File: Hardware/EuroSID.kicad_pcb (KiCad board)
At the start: 2 copper layers, 213.3 x 106.6 mm, 204 parts, among them J1 GATE_2, J10 IN_2, J11 IN_3, J12 PWM_CV, J13 Conn_01x04_Female, J14 Eurorack Connector, J15 Conn_01x06_Male, J16 Conn_ARM_JTAG_SWD_10, J2 GATE_3, J3 GATE_1, J4 OUT2_CON, J5 EXT_CON, J6 CUTOFF_CV, J7 SHAPE_CV, J8 OUT1_CON, J9 IN_1, Q1 MMBT3904, Q2 MMBT3904, Q3 MMBT3904, SW1 Frequency Adjust, SW10 FILTER_SW, SW11 FILTEREXT_SW, SW2 MOD_SW, SW3 FILTER1_SW, SW4 VOICE_SW, SW5 FILTER2_SW, SW6 PROG, SW7 RST, SW8 MODE_SW, SW9 FILTER3_SW, U1 TLC5947DAP, U10 LM1117-5.0, U11 L7809, U12 STM32F030R8Tx, U13 LM1117-3.3, U2 MCP6002-xSN, U3 MCP6004, U4 OPA1678, U5 MCP6002-xSN, U6 74HC595, U7 74HC595, U8 SID, U9 LM1117-3.3, X1 ECS-8FMX-010-TR

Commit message: Updated schematic
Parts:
- removed D28: LM4040DBZ-10, Package_TO_SOT_SMD:SOT-23
- added C69: 4.7 uF, Capacitor_Tantalum_SMD:CP_EIA-3216-18_Kemet-A, F.Cu at (107.4, 110.5)
- added D19: LP, LED_THT:LED_D3.0mm, F.Cu at (219.7, 49.5)
- added J17: Conn_ARM_JTAG_SWD_10, Connector_PinHeader_2.54mm:PinHeader_2x05_P2.54mm_Vertical, F.Cu at (59.7, 41.9)
- added R52: 120k, Resistor_SMD:R_0603_1608Metric, F.Cu at (135.9, 134.6)
- added R53: 1k, Resistor_SMD:R_0603_1608Metric, F.Cu at (110.4, 110.5)
- added R54: 1k, Resistor_SMD:R_0603_1608Metric, F.Cu at (107.4, 112.0)
- added R55: 1k, Resistor_SMD:R_0603_1608Metric, F.Cu at (110.4, 112.0)
- added SW12: FILTEREXT_SW, Button_Switch_THT:SW_PUSH_6mm_H9.5mm, F.Cu at (167.6, 86.4)
- C13, C22: value 18 pF -> 100 nF
- C14: value 100 nF -> 18 pF
- C23, C24: value 3.3 nF -> 100 nF
- C25, C26: value 2.2 nF -> 100 nF
- C27: value 2.2 nF -> 18 pF
- C29, C30: value 1 uF -> 3.3 nF; footprint Capacitor_Tantalum_SMD:CP_EIA-2012-12_Kemet-R -> Capacitor_SMD:C_0603_1608Metric
- C31: value 100 nF -> 2.2 nF
- C32: value 2200 uF -> 2.2 nF; footprint Capacitor_SMD:CP_Elec_10x10 -> Capacitor_SMD:C_0603_1608Metric
- C33: value 22 uF -> 2.2 nF; footprint Capacitor_SMD:CP_Elec_4x5.3 -> Capacitor_SMD:C_0603_1608Metric
- C34: value 22 uF -> 3.3 nF; footprint Capacitor_SMD:CP_Elec_4x5.3 -> Capacitor_SMD:C_0603_1608Metric
- C35, C36: value 22 uF -> 1 uF; footprint Capacitor_SMD:CP_Elec_4x5.3 -> Capacitor_Tantalum_SMD:CP_EIA-2012-12_Kemet-R
- C37, C47: value 22 uF -> 100 nF; footprint Capacitor_SMD:CP_Elec_4x5.3 -> Capacitor_SMD:C_0603_1608Metric
- C38: value 22 uF -> 2200 uF; footprint Capacitor_SMD:CP_Elec_4x5.3 -> Capacitor_SMD:CP_Elec_10x10
- C39, C40, C41, C44, C51: value 100 nF -> 22 uF; footprint Capacitor_SMD:C_0603_1608Metric -> Capacitor_SMD:CP_Elec_4x5.3
- C45: value 0.1 uF -> 22 uF; footprint Capacitor_SMD:C_0603_1608Metric -> Capacitor_SMD:CP_Elec_4x5.3
- C5: value 100 nF -> 0.1 uF
- C52: value 4.7 uF -> 22 uF; footprint Capacitor_Tantalum_SMD:CP_EIA-3216-18_Kemet-A -> Capacitor_SMD:CP_Elec_4x5.3
- C54: value 10 nF -> 100 nF
- C57, C65: value 100 nF -> 4.7 uF; footprint Capacitor_SMD:C_0603_1608Metric -> Capacitor_Tantalum_SMD:CP_EIA-3216-18_Kemet-A
- C58: value 1 uF -> 100 nF; footprint Capacitor_Tantalum_SMD:CP_EIA-2012-12_Kemet-R -> Capacitor_SMD:C_0603_1608Metric
- C59: value 10 uF -> 10 nF; footprint Capacitor_SMD:CP_Elec_4x5.7 -> Capacitor_SMD:C_0603_1608Metric
- C60: value 4.7 uF -> 100 nF; footprint Capacitor_Tantalum_SMD:CP_EIA-3216-18_Kemet-A -> Capacitor_SMD:C_0603_1608Metric
- C63: value 100 nF -> 1 uF; footprint Capacitor_SMD:C_0603_1608Metric -> Capacitor_Tantalum_SMD:CP_EIA-2012-12_Kemet-R
- C64: value 4.7 uF -> 10 uF; footprint Capacitor_Tantalum_SMD:CP_EIA-3216-18_Kemet-A -> Capacitor_SMD:CP_Elec_4x5.7
- D10: value BP -> TRIANGLE
- D11: value TRIANGLE -> DECAY
- D12: value DECAY -> VOICE3
- D13: value VOICE3 -> SID2
- D14: value SID2 -> FILTEREXT
- D15: value FILTEREXT -> MOD
- D16: value MOD -> SAW
- D17: value SAW -> SUSTAIN
- D18: value SUSTAIN -> FILTER1
- D2: value MODE_RG -> FILTER2; footprint LED_THT:LED_D3.0mm-3 -> LED_THT:LED_D3.0mm
- D20: value FILTER1 -> SYNC
- D21: value LP -> SYNC
- D22: value SYNC -> RELEASE
- D23: value SYNC -> MODE_RG; footprint LED_THT:LED_D3.0mm -> LED_THT:LED_D3.0mm-3
- D24: value RELEASE -> BZT52-C5V1J; footprint LED_THT:LED_D3.0mm -> Diode_SMD:D_SOD-123
- D25: value BZT52-C5V1J -> 1N5819HW-7-F
- D27: value 1N5819HW-7-F -> LM4040DBZ-10; footprint Diode_SMD:D_SOD-123 -> Package_TO_SOT_SMD:SOT-23
- D3: value FILTER2 -> HP
- D4: value HP -> SQUARE
- D5: value SQUARE -> ATTACK
- D6: value ATTACK -> VOICE2
- D7: value VOICE2 -> SID1
- D8: value SID1 -> FILTER3
- D9: value FILTER3 -> BP
- J13: value Conn_01x04_Female -> EXT_CON; footprint Connector_PinHeader_2.54mm:PinHeader_1x04_P2.54mm_Vertical -> Connector_Audio:Jack_3.5mm_QingPu_WQP-PJ398SM_Vertical_CircularHoles
- J14: value Eurorack Connector -> Conn_01x04_Female; footprint Connector_PinHeader_2.54mm:PinHeader_2x08_P2.54mm_Vertical -> Connector_PinHeader_2.54mm:PinHeader_1x04_P2.54mm_Vertical
- J15: value Conn_01x06_Male -> Eurorack Connector; footprint Connector_PinHeader_2.54mm:PinHeader_1x06_P2.54mm_Vertical -> Connector_PinHeader_2.54mm:PinHeader_2x08_P2.54mm_Vertical
- J16: value Conn_ARM_JTAG_SWD_10 -> Conn_01x06_Male; footprint Connector_PinHeader_2.54mm:PinHeader_2x05_P2.54mm_Vertical -> Connector_PinHeader_2.54mm:PinHeader_1x06_P2.54mm_Vertical
- J5: value EXT_CON -> CUTOFF_CV
- J6: value CUTOFF_CV -> SHAPE_CV
- J7: value SHAPE_CV -> SET_CV
- R25: value 30k -> 10k
- R26: value 1k -> 30k
- R27: value 50k -> 1k
- R35, R48: value 120k -> 100k
- R36, R51: value 1k -> 120k
- R37: value 180k -> 120k
- R38: value 100k -> 120k
- R39: value 180k -> 1k
- R40: value 100k -> 50k
- R43: value 120k -> 180k
- R45: value 47k -> 180k
- R46: value 47k -> 100k
- R49, R50: value 1k -> 47k
- RV6: value DECAY -> SUSTAIN
- RV7: value SUSTAIN -> DECAY
- SW10: value FILTER_SW -> SET_SW
- SW11: value FILTEREXT_SW -> FILTER_SW
- SW4: value VOICE_SW -> PROG; footprint Button_Switch_THT:SW_PUSH_6mm_H9.5mm -> Button_Switch_SMD:SW_SPST_EVPBF
- SW5: value FILTER2_SW -> VOICE_SW
- SW6: value PROG -> FILTER2_SW; footprint Button_Switch_SMD:SW_SPST_EVPBF -> Button_Switch_THT:SW_PUSH_6mm_H9.5mm
- U10: value LM1117-5.0 -> LM1117-3.3
- U11: value L7809 -> LM1117-5.0; footprint Package_TO_SOT_SMD:TO-252-3_TabPin2 -> Package_TO_SOT_SMD:SOT-223-3_TabPin2
- U12: value STM32F030R8Tx -> L7809; footprint Package_QFP:LQFP-64_10x10mm_P0.5mm -> Package_TO_SOT_SMD:TO-252-3_TabPin2
- U13: value LM1117-3.3 -> STM32F030R8Tx; footprint Package_TO_SOT_SMD:SOT-223-3_TabPin2 -> Package_QFP:LQFP-64_10x10mm_P0.5mm
- U2, U5: value MCP6002-xSN -> OPA1678
- U4: value OPA1678 -> MCP6004; footprint Package_SO:SOIC-8_3.9x4.9mm_P1.27mm -> Package_SO:TSSOP-14_4.4x5mm_P0.65mm
- moved SW6 188.5 mm to (48.3, 87.6)
- moved R12 165.4 mm to (72.6, 64.1)
- moved R15 165.4 mm to (72.6, 62.6)
- moved R19 165.4 mm to (54.5, 62.6)
- moved R2 165.4 mm to (54.5, 64.1)
- moved R22 165.4 mm to (63.6, 62.6)
- moved R6 165.4 mm to (63.6, 64.1)
- moved R1 165.4 mm to (60.6, 62.6)
- moved R11 165.4 mm to (75.6, 62.6)
- moved R14 165.4 mm to (69.6, 64.1)
- moved R16 165.4 mm to (69.6, 62.6)
- moved R17 165.4 mm to (66.6, 64.1)
- moved R20 165.4 mm to (66.6, 62.6)
- moved R23 165.4 mm to (60.6, 64.1)
- moved R3 165.4 mm to (57.5, 62.6)
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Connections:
- C10 pad 1: CUTOFF -> +3.3VA
- C11 pad 1: +3.3VA -> GND
- C12 pad 1: GND -> +3.3VA
- C13 pad 1: Net-(C13-Pad1) -> GND
- C13 pad 2: Net-(C13-Pad2) -> GND
- C14 pad 1: ATTACK -> Net-(C14-Pad1)
- C14 pad 2: GND -> Net-(C14-Pad2)
- C15 pad 1: DECAY -> ATTACK
- C17 pad 1: +12V -> DECAY
- C18 pad 1: GND -> +3.3VA
- C18 pad 2: -12V -> GND
- C19 pad 1: RELEASE -> GND
- C20 pad 1: +12V -> RELEASE
- C21 pad 1: GND -> +3.3VA
- C21 pad 2: -12V -> GND
- C22 pad 1: Net-(C22-Pad1) -> GND
- C22 pad 2: Net-(C22-Pad2) -> GND
- C23 pad 1: SHAPE_CV -> +12V
- C23 pad 2: Net-(C23-Pad2) -> GND
- C24 pad 1: CUTOFF_CV -> GND
- C24 pad 2: Net-(C24-Pad2) -> -12V
- C25 pad 1: IN1_CV -> +12V
- C25 pad 2: Net-(C25-Pad2) -> GND
- C26 pad 1: IN2_CV -> GND
- C26 pad 2: Net-(C26-Pad2) -> -12V
- C27 pad 1: IN3_CV -> Net-(C27-Pad1)
- C28 pad 1: PWM_CV -> SHAPE_CV
- C29 pad 1: SID1_OUT -> CUTOFF_CV
- C30 pad 1: SID1_EXT -> SET_CV
- C31 pad 1: +5V -> IN1_CV
- C31 pad 2: GND -> Net-(C31-Pad2)
- C32 pad 1: +5V -> IN2_CV
- C32 pad 2: GND -> Net-(C32-Pad2)
- C33 pad 1: Net-(C33-Pad1) -> IN3_CV
- C33 pad 2: GND -> Net-(C33-Pad2)
- C34 pad 1: Net-(C34-Pad1) -> PWM_CV
- C34 pad 2: GND -> Net-(C34-Pad2)
- C35 pad 1: Net-(C35-Pad1) -> SID1_OUT
- C35 pad 2: GND -> Net-(C35-Pad2)
- C36 pad 1: +3.3VA -> SID1_EXT
- C36 pad 2: GND -> Net-(C36-Pad2)
- C38 pad 1: +9V -> +5V
- C39 pad 1: +3.3VA -> Net-(C39-Pad1)
- C40 pad 1: +5V -> Net-(C40-Pad1)
- C41 pad 1: +9V -> Net-(C41-Pad1)
- C42 pad 1: +12V -> Net-(C42-Pad1)
- C43 pad 1: GND -> +3V3
- C43 pad 2: -12V -> GND
- C44 pad 1: -10V_REF -> +3.3VA
- C45 pad 1: RESET -> +5V
- C46 pad 1: Net-(C46-Pad1) -> +9V
- C48 pad 1: +3V3 -> +3.3VA
- C49 pad 1: +3V3 -> +5V
- C5 pad 1: +3.3VA -> RESET
- C50 pad 1: +3V3 -> +9V
- C51 pad 1: +3V3 -> +12V
- C52 pad 1: +3V3 -> GND
- C52 pad 2: GND -> -12V
- C53 pad 1: +3V3 -> -10V_REF
- C54 pad 1: +3.3VA -> +3V3
- C56 pad 1: +3.3VA -> +3V3
- C58 pad 1: +3.3VA -> +3V3
- C6 pad 1: GND -> RESONANCE
- C61 pad 1: +3V3 -> +3.3VA
- C63 pad 1: +3V3 -> +3.3VA
- C64 pad 1: +3V3 -> +3.3VA
- C65 pad 1: +3.3VA -> +3V3
- C66 pad 1: GND -> +3V3
- C67 pad 1: +3.3VA -> +3V3
- C68 pad 1: GND -> +3V3
- C7 pad 1: RESONANCE -> PWM
- C8 pad 1: PWM -> FREQ_ATTEN
- C9 pad 1: FREQ_ATTEN -> CUTOFF
- D24 pad 1: Net-(D24-Pad1) -> SID1_EXT
- D24 pad 2: +3V3 -> GND
- D25 pad 1: SID1_EXT -> +12V
- D25 pad 2: GND -> Net-(D25-Pad2)
- D26 pad 1: +12V -> Net-(D26-Pad1)
- D26 pad 2: Net-(D26-Pad2) -> -12V
- D27 pad 1: Net-(D27-Pad1) -> GND
- D27 pad 2: -12V -> -10V_REF
- FB1 pad 1: Net-(C33-Pad1) -> Net-(C39-Pad1)
- FB2 pad 1: Net-(C34-Pad1) -> Net-(C40-Pad1)
- FB3 pad 1: Net-(C35-Pad1) -> Net-(C41-Pad1)
- FB4 pad 1: Net-(C46-Pad1) -> Net-(C42-Pad1)
- J14 pad 1: Net-(D27-Pad1) -> Net-(J14-Pad1)
- J14 pad 2: Net-(D27-Pad1) -> Net-(J14-Pad2)
- J14 pad 3: GND -> Net-(J14-Pad3)
- J14 pad 4: GND -> Net-(J14-Pad4)
- J15 pad 1: GND -> Net-(D26-Pad1)
- J15 pad 2: Net-(J15-Pad2) -> Net-(D26-Pad1)
- J15 pad 3: Net-(J15-Pad3) -> GND
- J15 pad 4: RX -> GND
- J15 pad 5: TX -> GND
- J15 pad 6: Net-(J15-Pad6) -> GND
- J16 pad 1: +3V3 -> GND
- J16 pad 2: SWDIO -> (no net)
- J16 pad 3: GND -> (no net)
- J16 pad 4: SWCLK -> RX
- J16 pad 5: GND -> TX
- J16 pad 6: Net-(J16-Pad6) -> (no net)
- R16 pad 1: VOICE_SW -> PROG
- R17 pad 1: FILTER2_SW -> VOICE_SW
- R18 pad 1: PROG -> FILTER2_SW
- R22 pad 1: FILTER_SW -> SET_SW
- R23 pad 1: FILTEREXT_SW -> FILTER_SW
- R24 pad 1: Net-(C13-Pad2) -> FILTEREXT_SW
- R25 pad 1: Net-(C13-Pad2) -> Net-(C14-Pad2)
- R25 pad 2: Net-(C13-Pad1) -> GND
- R26 pad 1: Net-(C13-Pad1) -> Net-(C14-Pad2)
- R26 pad 2: Net-(J4-PadT) -> Net-(C14-Pad1)
- R27 pad 1: Net-(R27-Pad1) -> Net-(C14-Pad1)
- R27 pad 2: Net-(J5-PadT) -> Net-(J4-PadT)
- R28 pad 1: Net-(C22-Pad2) -> Net-(C27-Pad2)
- R29 pad 1: Net-(C22-Pad2) -> Net-(C27-Pad2)
- R29 pad 2: Net-(C22-Pad1) -> Net-(C27-Pad1)
- R30 pad 2: Net-(C23-Pad2) -> Net-(C28-Pad2)
- R31 pad 1: Net-(J7-PadT) -> Net-(J6-PadT)
- R31 pad 2: Net-(C23-Pad2) -> Net-(C28-Pad2)
- R32 pad 2: Net-(C24-Pad2) -> Net-(C29-Pad2)
- R33 pad 1: Net-(J6-PadT) -> Net-(J5-PadT)
- R33 pad 2: Net-(C24-Pad2) -> Net-(C29-Pad2)
- R34 pad 1: Net-(C23-Pad2) -> -10V_REF
- R34 pad 2: SHAPE_CV -> Net-(C30-Pad2)
- R35 pad 1: Net-(C24-Pad2) -> Net-(J7-PadT)
- R35 pad 2: CUTOFF_CV -> Net-(C30-Pad2)
- R36 pad 1: Net-(C22-Pad1) -> Net-(C28-Pad2)
- R36 pad 2: Net-(J8-PadT) -> SHAPE_CV
- R37 pad 1: -10V_REF -> Net-(C29-Pad2)
- R37 pad 2: Net-(C25-Pad2) -> CUTOFF_CV
- R38 pad 1: Net-(J10-PadTN) -> Net-(C30-Pad2)
- R38 pad 2: Net-(C25-Pad2) -> SET_CV
- R39 pad 1: -10V_REF -> Net-(C27-Pad1)
- R39 pad 2: Net-(C26-Pad2) -> Net-(J8-PadT)
- R40 pad 1: Net-(J10-PadT) -> Net-(R40-Pad1)
- R40 pad 2: Net-(C26-Pad2) -> Net-(J13-PadT)
- R41 pad 2: Net-(C27-Pad2) -> Net-(C31-Pad2)
- R42 pad 1: Net-(J11-PadT) -> Net-(J10-PadTN)
- R42 pad 2: Net-(C27-Pad2) -> Net-(C31-Pad2)
- R43 pad 2: Net-(C28-Pad2) -> Net-(C32-Pad2)
- R44 pad 1: Net-(J12-PadT) -> Net-(J10-PadT)
- R44 pad 2: Net-(C28-Pad2) -> Net-(C32-Pad2)
- R45 pad 1: Net-(C25-Pad2) -> -10V_REF
- R45 pad 2: IN1_CV -> Net-(C33-Pad2)
- R46 pad 1: Net-(C26-Pad2) -> Net-(J11-PadT)
- R46 pad 2: IN2_CV -> Net-(C33-Pad2)
- R47 pad 1: Net-(C27-Pad2) -> -10V_REF
- R47 pad 2: IN3_CV -> Net-(C34-Pad2)
- R48 pad 1: Net-(C28-Pad2) -> Net-(J12-PadT)
- R48 pad 2: PWM_CV -> Net-(C34-Pad2)
- R49 pad 1: GND -> Net-(C31-Pad2)
- R49 pad 2: Net-(C29-Pad2) -> IN1_CV
- R50 pad 1: -12V -> Net-(C32-Pad2)
- R50 pad 2: -10V_REF -> IN2_CV
- R51 pad 1: -12V -> Net-(C33-Pad2)
- R51 pad 2: -10V_REF -> IN3_CV
- RV6 pad 2: DECAY -> SUSTAIN
- RV7 pad 2: SUSTAIN -> DECAY
- RV9 pad 3: Net-(R27-Pad1) -> Net-(R40-Pad1)
- SW10 pad 2: FILTER_SW -> SET_SW
- SW11 pad 2: FILTEREXT_SW -> FILTER_SW
- SW4 pad 2: VOICE_SW -> PROG
- SW5 pad 2: FILTER2_SW -> VOICE_SW
- SW6 pad 2: PROG -> FILTER2_SW
- U1 pad 10: Net-(D8-Pad1) -> Net-(D7-Pad1)
- U1 pad 11: Net-(D14-Pad1) -> Net-(D13-Pad1)
- U1 pad 12: Net-(D20-Pad1) -> Net-(D18-Pad1)
- U1 pad 13: Net-(D3-Pad1) -> Net-(D2-Pad1)
- U1 pad 14: Net-(D9-Pad1) -> Net-(D8-Pad1)
- U1 pad 15: Net-(D15-Pad1) -> Net-(D14-Pad1)
- U1 pad 16: Net-(D21-Pad1) -> Net-(D19-Pad1)
- U1 pad 17: Net-(D4-Pad1) -> Net-(D3-Pad1)
- U1 pad 18: Net-(D10-Pad1) -> Net-(D9-Pad1)
- U1 pad 19: Net-(D16-Pad1) -> Net-(D15-Pad1)
- U1 pad 20: Net-(D22-Pad1) -> Net-(D20-Pad1)
- U1 pad 21: Net-(D5-Pad1) -> Net-(D4-Pad1)
- U1 pad 22: Net-(D11-Pad1) -> Net-(D10-Pad1)
- U1 pad 23: Net-(D17-Pad1) -> Net-(D16-Pad1)
- U1 pad 24: Net-(D23-Pad1) -> Net-(D21-Pad1)
- U1 pad 25: Net-(D6-Pad1) -> Net-(D5-Pad1)
- U1 pad 26: Net-(D12-Pad1) -> Net-(D11-Pad1)
- U1 pad 27: Net-(D18-Pad1) -> Net-(D17-Pad1)
- U1 pad 28: Net-(D24-Pad1) -> Net-(D22-Pad1)
- U1 pad 29: Net-(U1-Pad29) -> (no net)
- U1 pad 6: Net-(D7-Pad1) -> Net-(D6-Pad1)
- U1 pad 7: Net-(D13-Pad1) -> Net-(D12-Pad1)
- U1 pad 8: Net-(D2-Pad3) -> Net-(D23-Pad3)
- U1 pad 9: Net-(D2-Pad1) -> Net-(D23-Pad1)
- U10 pad 2: +5V -> +3.3VA
- U10 pad 3: Net-(C34-Pad1) -> Net-(C40-Pad1)
- U11 pad 1: Net-(C35-Pad1) -> GND
- U11 pad 2: GND -> +5V
- U11 pad 3: +9V -> Net-(C41-Pad1)
- U12 pad 1: +3V3 -> Net-(C42-Pad1)
- U12 pad 2: SID_RES -> GND
- U12 pad 3: SID_CS -> +9V
- U13 pad 1: GND -> +3V3
- U13 pad 2: +3V3 -> SID_RES
- U13 pad 3: Net-(C46-Pad1) -> SID_CS
- U2 pad 1: CUTOFF_CV -> Net-(C27-Pad1)
- U2 pad 2: Net-(C24-Pad2) -> Net-(C27-Pad2)
- U2 pad 3: GND -> SID1_OUT
- U2 pad 4: GND -> (no net)
- U2 pad 5: GND -> SID1_OUT
- U2 pad 6: Net-(C23-Pad2) -> Net-(C14-Pad2)
- U2 pad 7: SHAPE_CV -> Net-(C14-Pad1)
- U2 pad 8: +3.3VA -> (no net)
- U3 pad 1: IN1_CV -> SET_CV
- U3 pad 13: Net-(C28-Pad2) -> Net-(C34-Pad2)
- U3 pad 2: Net-(C25-Pad2) -> Net-(C30-Pad2)
- U3 pad 6: Net-(C26-Pad2) -> Net-(C29-Pad2)
- U3 pad 7: IN2_CV -> CUTOFF_CV
- U3 pad 8: IN3_CV -> SHAPE_CV
- U3 pad 9: Net-(C27-Pad2) -> Net-(C28-Pad2)
- U4 pad 1: Net-(C22-Pad1) -> IN1_CV
- U4 pad 2: Net-(C22-Pad2) -> Net-(C31-Pad2)
- U4 pad 3: SID1_OUT -> GND
- U4 pad 4: (no net) -> +3.3VA
- U4 pad 5: SID1_OUT -> GND
- U4 pad 6: Net-(C13-Pad2) -> Net-(C32-Pad2)
- U4 pad 7: Net-(C13-Pad1) -> IN2_CV
- U4 pad 8: (no net) -> IN3_CV
- U7 pad 5: Net-(U7-Pad5) -> (no net)
- U7 pad 6: Net-(U7-Pad6) -> (no net)
- U7 pad 7: Net-(U7-Pad7) -> (no net)
- U7 pad 9: Net-(U7-Pad9) -> (no net)
- U8 pad 1: Net-(J13-Pad4) -> Net-(J14-Pad4)
- U8 pad 2: Net-(J13-Pad3) -> Net-(J14-Pad3)
- U8 pad 23: Net-(U8-Pad23) -> (no net)
- U8 pad 24: Net-(U8-Pad24) -> (no net)
- U8 pad 26: Net-(C30-Pad2) -> Net-(C36-Pad2)
- U8 pad 27: Net-(C29-Pad2) -> Net-(C35-Pad2)
- U8 pad 3: Net-(J13-Pad2) -> Net-(J14-Pad2)
- U8 pad 4: Net-(J13-Pad1) -> Net-(J14-Pad1)
- U9 pad 2: +3.3VA -> +3V3
- U9 pad 3: Net-(C33-Pad1) -> Net-(C39-Pad1)

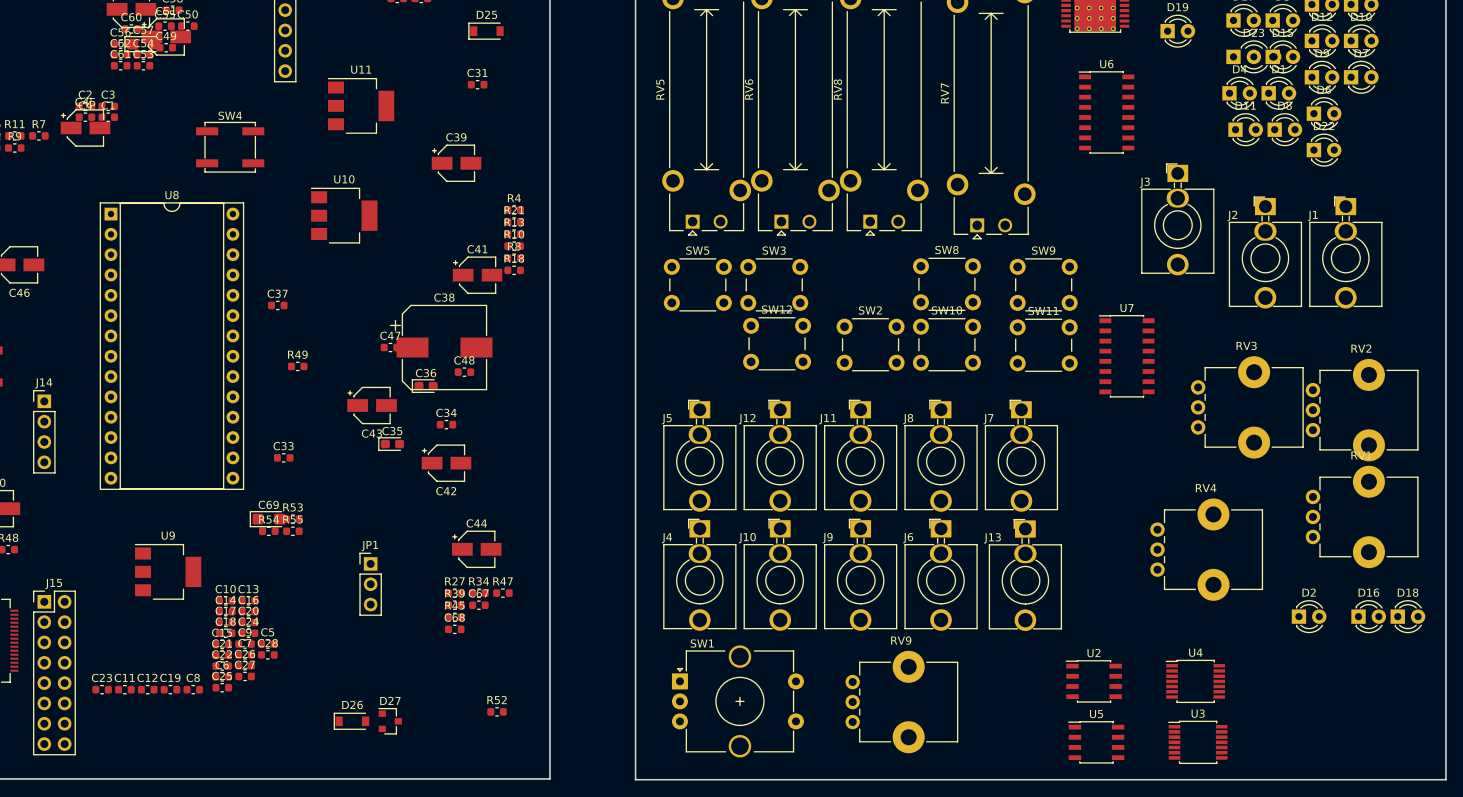
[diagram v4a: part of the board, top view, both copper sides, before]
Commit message: Fixed footprints for new attenuverter pots
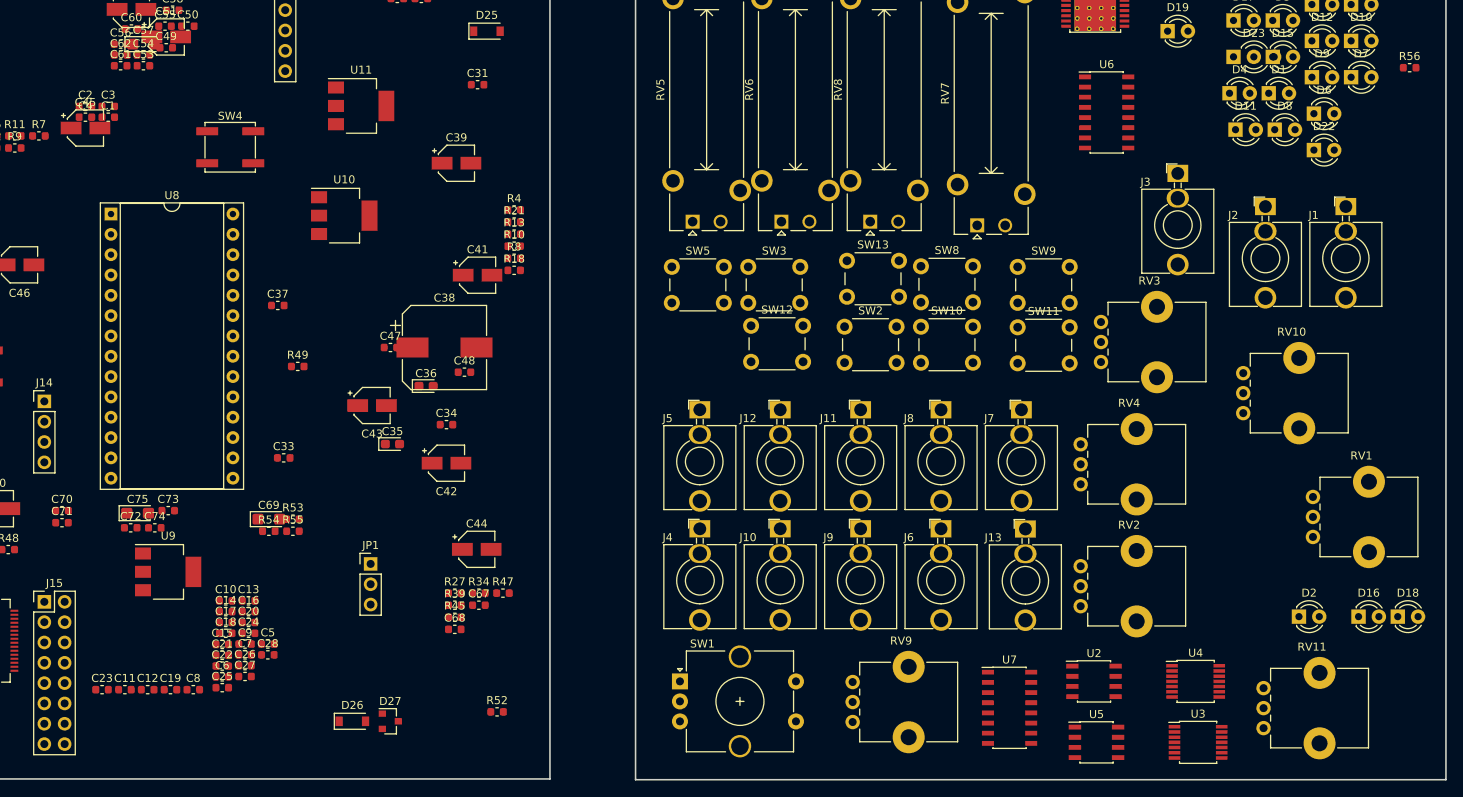
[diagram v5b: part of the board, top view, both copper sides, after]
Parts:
- added C70: 100 nF, Capacitor_SMD:C_0603_1608Metric, F.Cu at (81.5, 109.5)
- added C71: 100 nF, Capacitor_SMD:C_0603_1608Metric, F.Cu at (81.5, 111.0)
- added C72: 100 nF, Capacitor_SMD:C_0603_1608Metric, F.Cu at (90.1, 111.6)
- added C73: 100 nF, Capacitor_SMD:C_0603_1608Metric, F.Cu at (94.8, 109.5)
- added C74: 100 nF, Capacitor_SMD:C_0603_1608Metric, F.Cu at (93.1, 111.6)
- added C75: 4.7 uF, Capacitor_Tantalum_SMD:CP_EIA-3216-18_Kemet-A, F.Cu at (91.0, 109.8)
- added R56: 10k, Resistor_SMD:R_0603_1608Metric, F.Cu at (250.0, 54.1)
- added RV10: SET_ATTEN, Potentiometer_THT:Potentiometer_Bourns_PTV09A-1_Single_Vertical, F.Cu at (229.2, 97.3)
- added RV11: PWM_ATTEN, Potentiometer_THT:Potentiometer_Bourns_PTV09A-1_Single_Vertical, F.Cu at (231.7, 136.7)
- added SW13: SHAPE_SW, Button_Switch_THT:SW_PUSH_6mm_H9.5mm, F.Cu at (179.6, 78.2)
- U13: value STM32F030R8Tx -> STM32F303RBTx
- moved U7 46.3 mm to (199.9, 134.1)
- moved RV2 36.4 mm to (208.8, 121.4)
- moved RV3 14.6 mm to (211.4, 90.9)
- moved RV4 14.4 mm to (208.8, 106.2)
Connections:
- J1 pad TN: (no net) -> GND
- J10 pad TN: (no net) -> Net-(J10-PadTN)
- J11 pad TN: (no net) -> Net-(J10-PadT)
- J12 pad TN: (no net) -> GND
- J13 pad TN: (no net) -> GND
- J2 pad TN: (no net) -> GND
- J3 pad TN: (no net) -> GND
- J5 pad TN: (no net) -> GND
- J6 pad TN: (no net) -> GND
- J7 pad TN: (no net) -> GND
- J9 pad TN: (no net) -> GND
- U13 pad 1: +3V3 -> (no net)
- U13 pad 18: MOD_SW -> CUTOFF_CV
- U13 pad 19: VOICE_SW -> +3V3
- U13 pad 20: CUTOFF_CV -> SHAPE_CV
- U13 pad 21: SHAPE_CV -> PWM_CV
- U13 pad 22: IN1_CV -> PWM_ATTEN
- U13 pad 23: IN2_CV -> SET_CV
- U13 pad 24: SET_CV -> SET_ATTEN
- U13 pad 25: FILTER_SW -> IN3_CV
- U13 pad 26: IN3_CV -> IN1_CV
- U13 pad 27: PWM_CV -> IN2_CV
- U13 pad 28: FILTER1_SW -> GATE_1
- U13 pad 29: FILTER2_SW -> GATE_2
- U13 pad 30: FILTER3_SW -> GATE_3
- U13 pad 35: FILTEREXT_SW -> VOICE_SW
- U13 pad 37: GATE_1 -> FILTER_SW
- U13 pad 38: GATE_2 -> FILTEREXT_SW
- U13 pad 39: GATE_3 -> FILTER3_SW
- U13 pad 40: (no net) -> FILTER2_SW
- U13 pad 41: MODE_SW -> FILTER1_SW
- U13 pad 44: SET_SW -> SHAPE_SW
- U13 pad 45: (no net) -> SET_SW
- U13 pad 47: (no net) -> GND
- U13 pad 48: (no net) -> +3V3
- U13 pad 51: (no net) -> MOD_SW
- U13 pad 52: (no net) -> MODE_SW

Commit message: Board 1 Complete
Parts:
- removed U5: OPA1678, Package_SO:SOIC-8_3.9x4.9mm_P1.27mm
- moved R17 168.4 mm to (192.6, 175.9)
- moved R5 168.4 mm to (183.5, 175.9)
- moved R9 168.4 mm to (201.6, 175.9)
- moved C29 168.4 mm to (194.8, 167.2)
- moved C32 168.4 mm to (179.2, 163.8)
- moved R1 168.4 mm to (186.5, 174.4)
- moved R11 168.4 mm to (201.6, 174.4)
- moved R12 168.4 mm to (198.6, 175.9)
- moved R14 168.4 mm to (195.6, 175.9)
- moved R15 168.4 mm to (198.6, 174.4)
- moved R16 168.4 mm to (195.6, 174.4)
- moved R19 168.4 mm to (180.5, 174.4)
- moved R2 168.4 mm to (180.5, 175.9)
- moved R20 168.4 mm to (192.6, 174.4)
- moved R22 168.4 mm to (189.5, 174.4)
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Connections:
- U2 pad 4: (no net) -> -12V
- U2 pad 8: (no net) -> +12V
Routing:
- net +3V3: track 0.00 -> 170.8 mm, vias 0 -> 4
- net +5V: track 0.00 -> 146.1 mm, vias 0 -> 4
- net +3.3VA: track 0.00 -> 75.0 mm, vias 0 -> 2
- net SID_LATCH: track 0.00 -> 72.6 mm, vias 0 -> 2
- net SID_RES: track 0.00 -> 68.6 mm, vias 0 -> 2
- net SID_CS: track 0.00 -> 61.4 mm, vias 0 -> 2
- net SID_DATA: track 0.00 -> 55.5 mm, vias 0 -> 2
- net SID_CLK: track 0.00 -> 54.7 mm, vias 0 -> 2
- net +12V: track 0.00 -> 49.5 mm
- net GND: track 0.00 -> 48.0 mm
- net /SID Chip/A0: track 0.00 -> 39.2 mm
- net /SID Chip/A1: track 0.00 -> 35.6 mm
- net /SID Chip/A2: track 0.00 -> 32.3 mm
- net RESET: track 0.00 -> 31.5 mm
- net /SID Chip/A3: track 0.00 -> 29.1 mm
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- added copper zone on B.Cu, net GND
- added copper zone on F.Cu, net GND

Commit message: Seperated two board with headers
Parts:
- added J18: Power_Connector_IO, Connector_PinSocket_2.54mm:PinSocket_1x07_P2.54mm_Vertical_SMD_Pin1Left, B.Cu at (161.0, 49.0)
- added J19: Power_Connector, Connector_PinHeader_2.54mm:PinHeader_1x07_P2.54mm_Vertical, B.Cu at (52.6, 58.7)
- added J20: Digital_Connector_IO, Connector_PinSocket_2.54mm:PinSocket_2x11_P2.54mm_Vertical_SMD, B.Cu at (175.6, 54.1)
- added J21: CV_Connector_IO, Connector_PinSocket_2.54mm:PinSocket_2x04_P2.54mm_Vertical_SMD, B.Cu at (193.8, 47.2)
- added J22: Pot_Connector_IO, Connector_PinSocket_2.54mm:PinSocket_2x04_P2.54mm_Vertical_SMD, B.Cu at (209.6, 63.5)
- added J23: Attenuverter_Connector_IO, Connector_PinSocket_2.54mm:PinSocket_1x04_P2.54mm_Vertical_SMD_Pin1Left, B.Cu at (197.4, 63.8)
- added J24: Digital_Connector, Connector_PinHeader_2.54mm:PinHeader_2x11_P2.54mm_Vertical, F.Cu at (63.3, 43.4)
- added J25: CV_Connector, Connector_PinSocket_2.54mm:PinSocket_2x04_P2.54mm_Vertical, F.Cu at (52.6, 68.3)
- added J26: Pot_Connector, Connector_PinSocket_2.54mm:PinSocket_2x04_P2.54mm_Vertical, F.Cu at (65.8, 79.5)
- added J27: Attenuverter_Connector, Connector_PinSocket_2.54mm:PinSocket_1x04_P2.54mm_Vertical, F.Cu at (51.1, 87.1)
- added J28: SID_Audio_Connector_IO, Connector_PinSocket_2.54mm:PinSocket_1x04_P2.54mm_Vertical_SMD_Pin1Left, B.Cu at (161.7, 67.1)
- added J29: SID_Audio_Connector, Connector_PinHeader_2.54mm:PinHeader_1x04_P2.54mm_Vertical, F.Cu at (133.9, 55.1)
- U1, U2, U3, U4: moved to B.Cu
- moved C33 276.3 mm to (264.7, 43.9)
- moved C4 276.3 mm to (287.6, 49.1)
- moved R10 276.3 mm to (291.4, 36.3)
- moved R13 276.3 mm to (291.4, 34.8)
- moved R18 276.3 mm to (291.4, 39.3)
- moved R21 276.3 mm to (291.4, 33.3)
- moved R4 276.3 mm to (291.4, 31.7)
- moved R49 276.3 mm to (266.4, 32.5)
- moved R8 276.3 mm to (291.4, 37.8)
- moved C34 276.3 mm to (285.0, 39.8)
- moved Q3 249.3 mm to (273.3, 98.4)
- moved Q1 249.3 mm to (266.4, 98.4)
- moved Q2 249.3 mm to (269.8, 98.4)
- moved D24 242.2 mm to (267.0, 152.1)
- moved R37 219.8 mm to (218.1, 23.8)
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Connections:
- C1 pad 1: FREQ_A -> FREQ_A_IO
- C10 pad 1: +3.3VA -> 3.3A_IO
- C12 pad 1: +3.3VA -> 3.3A_IO
- C15 pad 1: ATTACK -> ATTACK_IO
- C16 pad 1: SUSTAIN -> SUSTAIN_IO
- C17 pad 1: DECAY -> DECAY_IO
- C18 pad 1: +3.3VA -> 3.3A_IO
- C2 pad 2: FREQ_B -> FREQ_B_IO
- C20 pad 1: RELEASE -> RELEASE_IO
- C21 pad 1: +3.3VA -> 3.3A_IO
- C23 pad 1: +12V -> 12V_IO
- C24 pad 2: -12V -> -12V_IO
- C25 pad 1: +12V -> 12V_IO
- C26 pad 2: -12V -> -12V_IO
- C28 pad 1: SHAPE_CV -> SHAPE_CV_IO
- C29 pad 1: CUTOFF_CV -> CUTOFF_CV_IO
- C3 pad 1: +5V -> 5V_IO
- C30 pad 1: SET_CV -> SET_CV_IO
- C31 pad 1: IN1_CV -> IN1_CV_IO
- C32 pad 1: IN2_CV -> IN2_CV_IO
- C33 pad 1: IN3_CV -> IN3_CV_IO
- C34 pad 1: PWM_CV -> PWM_CV_IO
- C4 pad 1: FREQ_SW -> FREQ_SW_IO
- C4 pad 2: +3V3 -> 3.3_IO
- C6 pad 1: RESONANCE -> RESONANCE_IO
- C7 pad 1: PWM -> PWM_IO
- C70 pad 1: SET_ATTEN -> SET_ATTEN_IO
- C71 pad 1: PWM_ATTEN -> PWM_ATTEN_IO
- C8 pad 1: FREQ_ATTEN -> FREQ_ATTEN_IO
- C9 pad 1: CUTOFF -> CUTOFF_IO
- D1 pad 2: +3V3 -> 3.3_IO
- D10 pad 2: +3V3 -> 3.3_IO
- D11 pad 2: +3V3 -> 3.3_IO
- D12 pad 2: +3V3 -> 3.3_IO
- D13 pad 2: +3V3 -> 3.3_IO
- D14 pad 2: +3V3 -> 3.3_IO
- D15 pad 2: +3V3 -> 3.3_IO
- D16 pad 2: +3V3 -> 3.3_IO
- D17 pad 2: +3V3 -> 3.3_IO
- D18 pad 2: +3V3 -> 3.3_IO
- D19 pad 2: +3V3 -> 3.3_IO
- D2 pad 2: +3V3 -> 3.3_IO
- D20 pad 2: +3V3 -> 3.3_IO
- D21 pad 2: +3V3 -> 3.3_IO
- D22 pad 2: +3V3 -> 3.3_IO
- D23 pad 2: +3V3 -> 3.3_IO
- D24 pad 1: SID1_EXT -> SID1_EXT_IO
- D3 pad 2: +3V3 -> 3.3_IO
- D4 pad 2: +3V3 -> 3.3_IO
- D5 pad 2: +3V3 -> 3.3_IO
- D6 pad 2: +3V3 -> 3.3_IO
- D7 pad 2: +3V3 -> 3.3_IO
- D8 pad 2: +3V3 -> 3.3_IO
- D9 pad 2: +3V3 -> 3.3_IO
- Q1 pad 3: GATE_1 -> GATE_1_IO
- Q2 pad 3: GATE_2 -> GATE_2_IO
- Q3 pad 3: GATE_3 -> GATE_3_IO
- R11 pad 1: +3V3 -> 3.3_IO
- R11 pad 2: GATE_1 -> GATE_1_IO
- R12 pad 1: +3V3 -> 3.3_IO
- R12 pad 2: GATE_2 -> GATE_2_IO
- R13 pad 1: +3V3 -> 3.3_IO
- R13 pad 2: GATE_3 -> GATE_3_IO
- R14 pad 1: MOD_SW -> MOD_SW_IO
- R15 pad 1: FILTER1_SW -> FILTER1_SW_IO
- R17 pad 1: VOICE_SW -> VOICE_SW_IO
- R18 pad 1: FILTER2_SW -> FILTER2_SW_IO
- R2 pad 2: FREQ_A -> FREQ_A_IO
- R20 pad 1: MODE_SW -> MODE_SW_IO
- R21 pad 1: FILTER3_SW -> FILTER3_SW_IO
- R22 pad 1: SET_SW -> SET_SW_IO
- R23 pad 1: FILTER_SW -> FILTER_SW_IO
- R24 pad 1: FILTEREXT_SW -> FILTEREXT_SW_IO
- R3 pad 2: FREQ_B -> FREQ_B_IO
- R30 pad 1: -10V_REF -> -10V_REF_IO
- R32 pad 1: -10V_REF -> -10V_REF_IO
- R34 pad 1: -10V_REF -> -10V_REF_IO
- R36 pad 2: SHAPE_CV -> SHAPE_CV_IO
- R37 pad 2: CUTOFF_CV -> CUTOFF_CV_IO
- R38 pad 2: SET_CV -> SET_CV_IO
- R4 pad 2: +3V3 -> 3.3_IO
- R41 pad 1: -10V_REF -> -10V_REF_IO
- R43 pad 1: -10V_REF -> -10V_REF_IO
- R45 pad 1: -10V_REF -> -10V_REF_IO
- R47 pad 1: -10V_REF -> -10V_REF_IO
- R49 pad 2: IN1_CV -> IN1_CV_IO
- R5 pad 1: +3V3 -> 3.3_IO
- R50 pad 2: IN2_CV -> IN2_CV_IO
- R51 pad 2: IN3_CV -> IN3_CV_IO
- R52 pad 2: PWM_CV -> PWM_CV_IO
- R56 pad 1: SHAPE_SW -> SHAPE_SW_IO
- R7 pad 2: FREQ_SW -> FREQ_SW_IO
- RV1 pad 1: +3V3 -> 3.3A_IO
- RV1 pad 2: RESONANCE -> RESONANCE_IO
- RV10 pad 1: +3V3 -> 3.3A_IO
- RV10 pad 2: SET_ATTEN -> SET_ATTEN_IO
- RV11 pad 1: +3V3 -> 3.3A_IO
- RV11 pad 2: PWM_ATTEN -> PWM_ATTEN_IO
- RV2 pad 1: +3V3 -> 3.3A_IO
- RV2 pad 2: PWM -> PWM_IO
- RV3 pad 1: +3V3 -> 3.3A_IO
- RV3 pad 2: FREQ_ATTEN -> FREQ_ATTEN_IO
- RV4 pad 1: +3V3 -> 3.3A_IO
- RV4 pad 2: CUTOFF -> CUTOFF_IO
- RV5 pad 1: +3V3 -> 3.3A_IO
- RV5 pad 2: ATTACK -> ATTACK_IO
- RV6 pad 1: +3V3 -> 3.3A_IO
- RV6 pad 2: SUSTAIN -> SUSTAIN_IO
- RV7 pad 1: +3V3 -> 3.3A_IO
- RV7 pad 2: DECAY -> DECAY_IO
- RV8 pad 1: +3V3 -> 3.3A_IO
- RV8 pad 2: RELEASE -> RELEASE_IO
- RV9 pad 2: SID1_EXT -> SID1_EXT_IO
- SW1 pad S2: +3V3 -> 3.3_IO
- SW10 pad 1: +3V3 -> 3.3_IO
- SW10 pad 2: SET_SW -> SET_SW_IO
- SW11 pad 1: +3V3 -> 3.3_IO
- SW11 pad 2: FILTER_SW -> FILTER_SW_IO
- SW12 pad 1: +3V3 -> 3.3_IO
- SW12 pad 2: FILTEREXT_SW -> FILTEREXT_SW_IO
- SW13 pad 1: +3V3 -> 3.3_IO
- SW13 pad 2: SHAPE_SW -> SHAPE_SW_IO
- SW2 pad 1: +3V3 -> 3.3_IO
- SW2 pad 2: MOD_SW -> MOD_SW_IO
- SW3 pad 1: +3V3 -> 3.3_IO
- SW3 pad 2: FILTER1_SW -> FILTER1_SW_IO
- SW5 pad 1: +3V3 -> 3.3_IO
- SW5 pad 2: VOICE_SW -> VOICE_SW_IO
- SW6 pad 1: +3V3 -> 3.3_IO
- SW6 pad 2: FILTER2_SW -> FILTER2_SW_IO
- SW8 pad 1: +3V3 -> 3.3_IO
- SW8 pad 2: MODE_SW -> MODE_SW_IO
- SW9 pad 1: +3V3 -> 3.3_IO
- SW9 pad 2: FILTER3_SW -> FILTER3_SW_IO
- U1 pad 3: LED_CLK -> LED_CLK_IO
- U1 pad 30: LED_LATCH -> LED_LATCH_IO
- U1 pad 32: +5V -> 5V_IO
- U1 pad 4: LED_DATA -> LED_DATA_IO
- U2 pad 3: SID1_OUT -> SID1_OUT_IO
- U2 pad 4: -12V -> -12V_IO
- U2 pad 5: SID1_OUT -> SID2_OUT_IO
- U2 pad 8: +12V -> 12V_IO
- U3 pad 1: SET_CV -> SET_CV_IO
- U3 pad 14: PWM_CV -> PWM_CV_IO
- U3 pad 4: +3.3VA -> 3.3A_IO
- U3 pad 7: CUTOFF_CV -> CUTOFF_CV_IO
- U3 pad 8: SHAPE_CV -> SHAPE_CV_IO
- U4 pad 1: IN1_CV -> IN1_CV_IO
- U4 pad 4: +3.3VA -> 3.3A_IO
- U4 pad 7: IN2_CV -> IN2_CV_IO
- U4 pad 8: IN3_CV -> IN3_CV_IO
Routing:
- net +3V3: track 170.8 -> 180.9 mm, vias 4 -> 5
- net PROG: track 23.1 -> 33.0 mm
- net RESET: track 31.5 -> 41.3 mm
- net GND: track 48.0 -> 55.6 mm
